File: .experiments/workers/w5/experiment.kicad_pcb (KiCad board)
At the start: 2 copper layers, 140 x 90 mm, 39 parts, among them J1 USB_C, J2 Output, J3 Debug, Q1 FS8205A, U1 USBLC6-2SC6, U2 BQ24072, U3 HY2113-KB5B, U4 MT3608, U5 AP2112K-3.3, U6 LN61CN3302MR-G

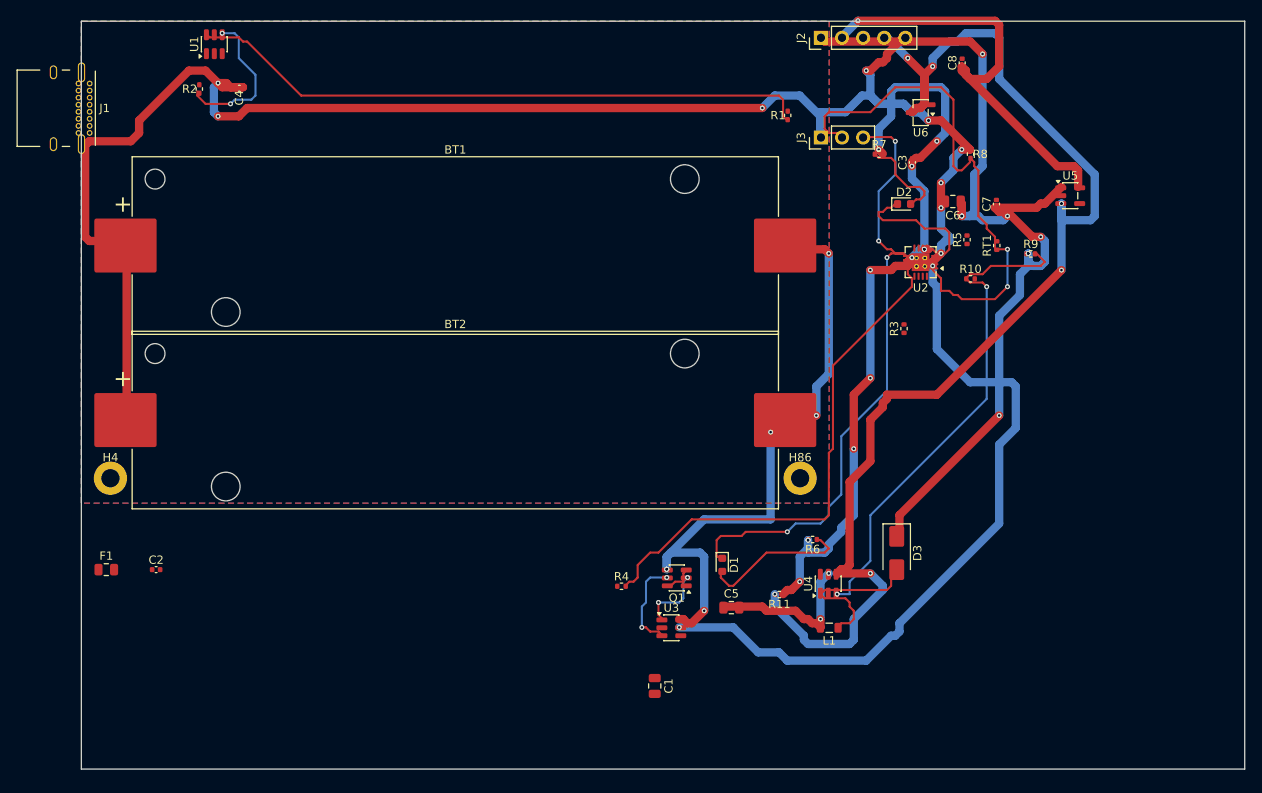
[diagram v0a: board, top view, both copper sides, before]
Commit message: 35-round experiment: best score 25.33, improved routing params
Router and conflict resolution tuning from autonomous optimization loop.
Best config: clearance=0.2051mm, cooling_factor=0.9735, existing_trace_cost=200.0

Co-Authored-By: Claude Opus 4.6 <noreply@anthropic.com>
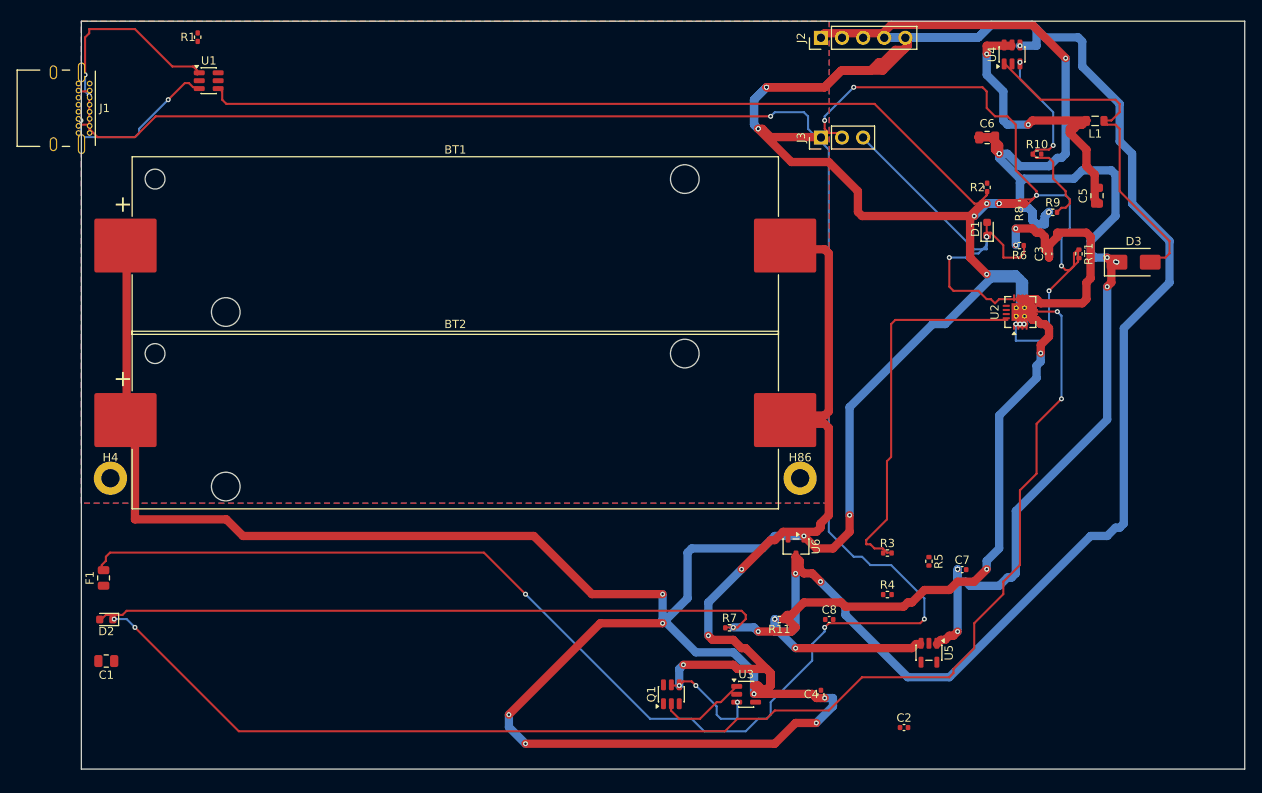
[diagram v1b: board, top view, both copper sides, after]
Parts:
- moved D2 108.2 mm to (3.00, 72.0), turned to 180 degrees
- moved C4 101.1 mm to (89.0, 81.0), turned to 90 degrees
- moved R2 95.5 mm to (109.0, 20.0)
- moved C2 92.0 mm to (99.0, 85.0)
- moved R1 71.6 mm to (14.0, 1.92)
- moved C8 68.9 mm to (90.0, 72.0), turned to 0 degrees
- moved L1 68.9 mm to (122.0, 12.0)
- moved U4 67.4 mm to (112.0, 4.00)
- moved C5 66.3 mm to (122.2, 21.0), turned to 90 degrees
- moved C1 66.1 mm to (3.00, 77.0), turned to 180 degrees
- moved R7 59.8 mm to (78.0, 73.0)
- moved U5 57.6 mm to (102.0, 76.0), turned to -90 degrees
- moved U6 54.3 mm to (86.0, 63.2), turned to -90 degrees
- moved D1 51.5 mm to (109.0, 25.0), turned to 90 degrees
- moved D3 45.1 mm to (126.6, 29.0), turned to 0 degrees
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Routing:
- net Net-(F1-Pad2): track 0.00 -> 280.5 mm, vias 0 -> 4
- net Net-(D2-K): track 18.7 -> 161.6 mm, vias 0 -> 4
- net /VBAT: track 293.0 -> 399.7 mm, vias 14 -> 20
- net Net-(R2-Pad1): track 18.4 -> 99.8 mm, vias 2 -> 0
- net Net-(R1-Pad1): track 75.5 -> 0.00 mm
- net Net-(D2-A): track 11.2 -> 81.5 mm
- net Net-(U2-ILIM): track 62.7 -> 0.00 mm
- net /5V: track 115.5 -> 171.2 mm, vias 8 -> 12
- net /3V3: track 52.5 -> 0.00 mm, vias 2 -> 0
- net /EN: track 149.0 -> 200.2 mm
- net Net-(U2-ISET): track 0.00 -> 45.4 mm
- net Net-(U4-FB): track 60.0 -> 25.2 mm
- net /CHG_N: track 75.4 -> 42.2 mm
- net /CELL_NEG: track 75.5 -> 101.2 mm, vias 6 -> 4
- net Net-(J1-CC1): track 0.00 -> 24.0 mm, vias 0 -> 2
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
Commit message: 45-round experiment: best score 25.66, all nets routed (26/26)
Fixed A* performance by increasing max_search from 100k->500k to handle
high trace costs (100.0) without timing out. Kept high cost + coarse grid
(0.5mm) to prevent shorts while still routing efficiently.

Best config: edge_margin=5.7493mm, cooling_factor=0.9764, existing_trace_cost=200, max_rips=8

Co-Authored-By: Claude Opus 4.6 <noreply@anthropic.com>
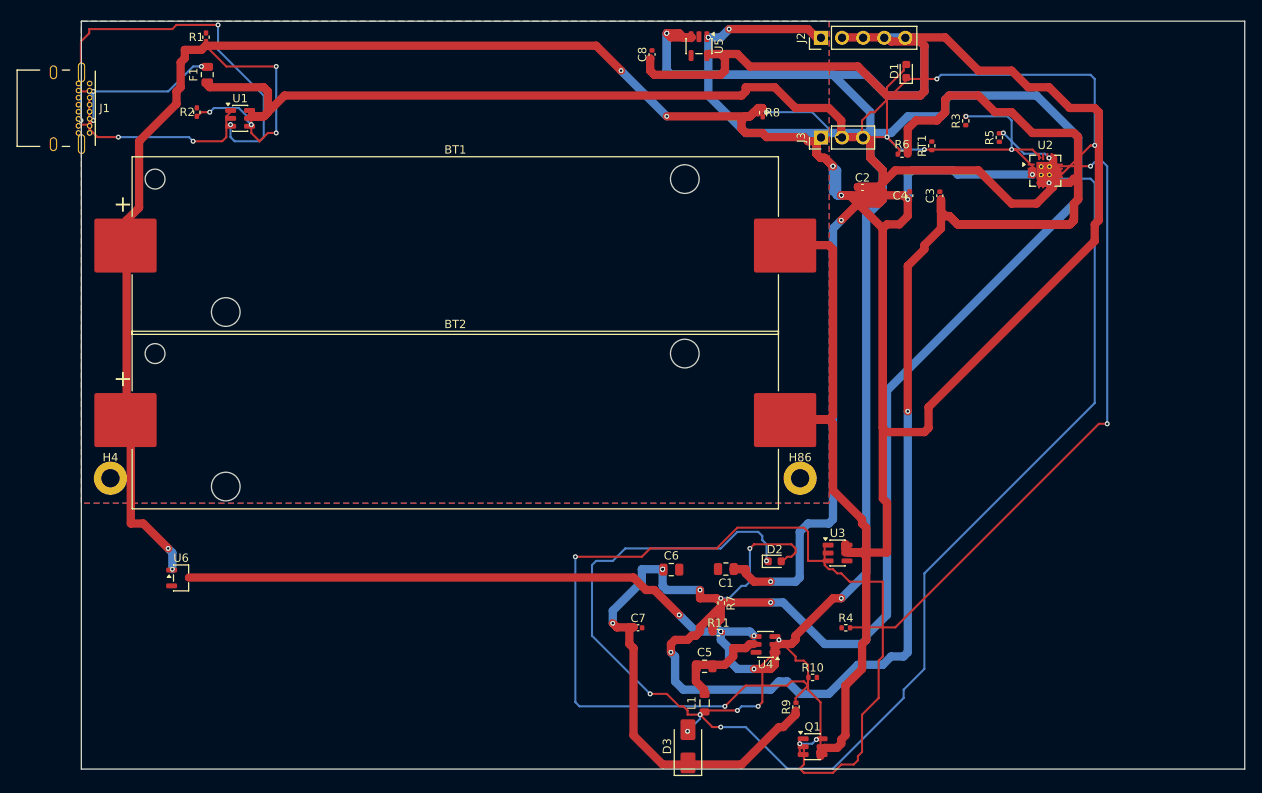
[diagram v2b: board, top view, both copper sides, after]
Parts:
- moved R2 95.5 mm to (13.9, 10.9)
- moved L1 84.4 mm to (75.0, 82.1), turned to 90 degrees
- moved D2 80.7 mm to (83.4, 65.0), turned to 0 degrees
- moved D3 79.2 mm to (73.0, 87.3), turned to 90 degrees
- moved U5 78.1 mm to (74.3, 3.00)
- moved U4 76.9 mm to (82.3, 75.0), turned to 180 degrees
- moved C1 75.4 mm to (77.6, 65.9)
- moved U6 74.1 mm to (12.0, 67.0), turned to 0 degrees
- moved C5 73.7 mm to (75.0, 77.6), turned to 0 degrees
- moved C8 71.3 mm to (68.7, 4.00), turned to 90 degrees
- moved R10 68.5 mm to (88.0, 79.0)
- moved R9 67.1 mm to (86.0, 82.5), turned to 90 degrees
- moved C2 65.2 mm to (94.0, 20.0)
- moved C6 64.4 mm to (71.0, 66.0)
- moved F1 61.8 mm to (15.2, 6.43)
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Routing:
- net Net-(F1-Pad2): track 280.5 -> 21.7 mm
- net /VBUS: track 0.00 -> 197.8 mm, vias 0 -> 2
- net Net-(R2-Pad1): track 99.8 -> 8.04 mm, vias 0 -> 2
- net /VSYS: track 107.0 -> 191.5 mm, vias 6 -> 2
- net Net-(U2-ILIM): track 0.00 -> 78.6 mm, vias 0 -> 2
- net Net-(Q1B-G): track 12.7 -> 90.9 mm
- net Net-(D2-A): track 81.5 -> 16.7 mm, vias 0 -> 2
- net /3V3: track 0.00 -> 58.8 mm
- net /5V: track 171.2 -> 224.6 mm, vias 12 -> 9
- net /NTC_SENSE: track 81.7 -> 35.4 mm, vias 6 -> 4
- net /EN: track 200.2 -> 240.3 mm, vias 8 -> 10
- net /VBAT: track 399.7 -> 362.0 mm, vias 20 -> 10
- net Net-(Q1A-G): track 11.1 -> 44.1 mm
- net Net-(U2-ISET): track 45.4 -> 13.1 mm, vias 0 -> 2
- net Net-(J1-CC2): track 19.2 -> 48.8 mm, vias 2 -> 4
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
